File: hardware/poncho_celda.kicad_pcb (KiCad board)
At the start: 2 copper layers, 20 parts, among them U1 AD620, U2 REF1004-2.5, U3 ADS1113/15

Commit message: Primera version de de diseño de PCB, terminado.
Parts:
- moved C3 28.8 mm to (103.6, 115.2)
- moved R4 28.8 mm to (129.2, 138.6)
- moved U2 28.8 mm to (136.8, 132.2)
- moved C6 28.8 mm to (133.6, 122.0)
- moved C1 28.8 mm to (103.6, 118.5)
- moved C2 28.8 mm to (113.3, 124.6)
- moved C4 28.8 mm to (118.6, 123.1)
- moved R5 28.8 mm to (131.1, 108.3)
- moved U1 28.8 mm to (113.3, 117.0)
- moved U3 28.8 mm to (129.2, 117.0)
- moved R6 28.8 mm to (134.4, 108.3)
- moved C5 28.8 mm to (99.3, 139.1)
- moved R1 28.8 mm to (109.5, 130.9)
- moved R2 28.8 mm to (117.1, 130.9)
- moved R3 28.8 mm to (113.3, 111.1)
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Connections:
- R5 pad 1: +3.3V -> +3V3
- R6 pad 1: +3.3V -> +3V3
- XA1 pad 1: Net-(XA1-Pad1) -> +3V3
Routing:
- net +3V3: track 0.00 -> 38.9 mm
- net /lcd/RS: track 78.6 -> 106.6 mm, vias 2 -> 0
- net +5V: track 304.4 -> 281.4 mm
- net GND: track 251.9 -> 230.0 mm, vias 5 -> 3
- net /lcd/Ena: track 98.4 -> 120.1 mm
- net /ADC/sda: track 33.9 -> 44.8 mm, vias 0 -> 1
- net /ADC/alert: track 59.7 -> 50.2 mm, vias 0 -> 1
- net Net-(DS1-Pad16): track 6.73 -> 15.8 mm
- net /ADC/scl: track 28.1 -> 35.1 mm
- net /lcd/D2: track 65.9 -> 60.4 mm
- net /lcd/D1: track 68.6 -> 63.1 mm
- net /lcd/D4: track 59.0 -> 53.5 mm
- net /lcd/D3: track 63.0 -> 57.5 mm
- net Net-(DS1-Pad3): track 12.3 -> 10.8 mm
- added copper zone on F.Cu, net +5V
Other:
- board outline added: 85.9 x 137 mm

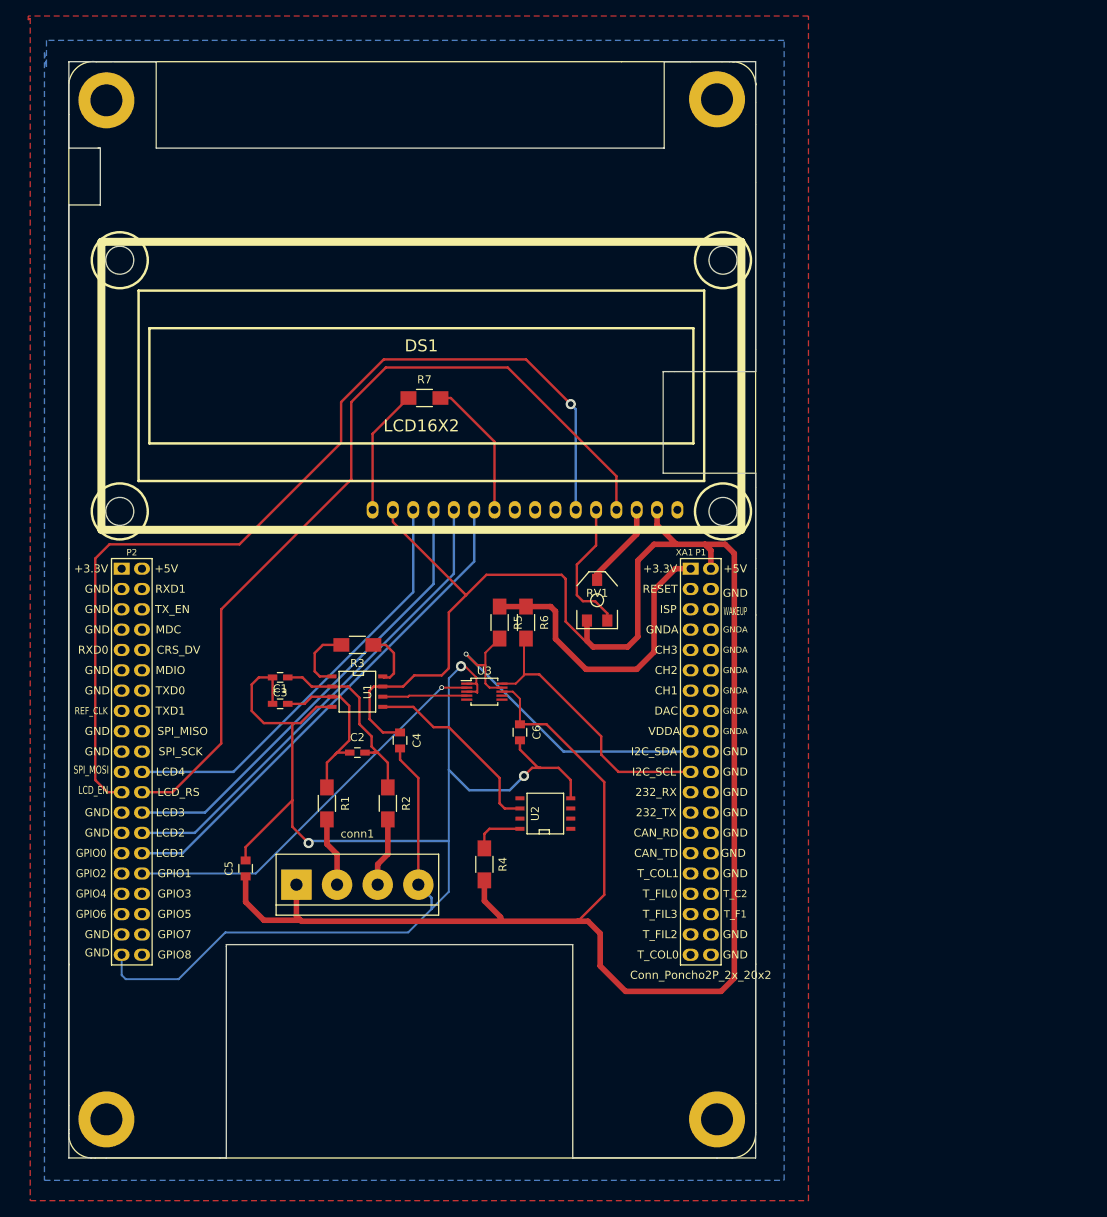
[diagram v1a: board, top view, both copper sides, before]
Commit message: Se realizan correcciones de PCB.
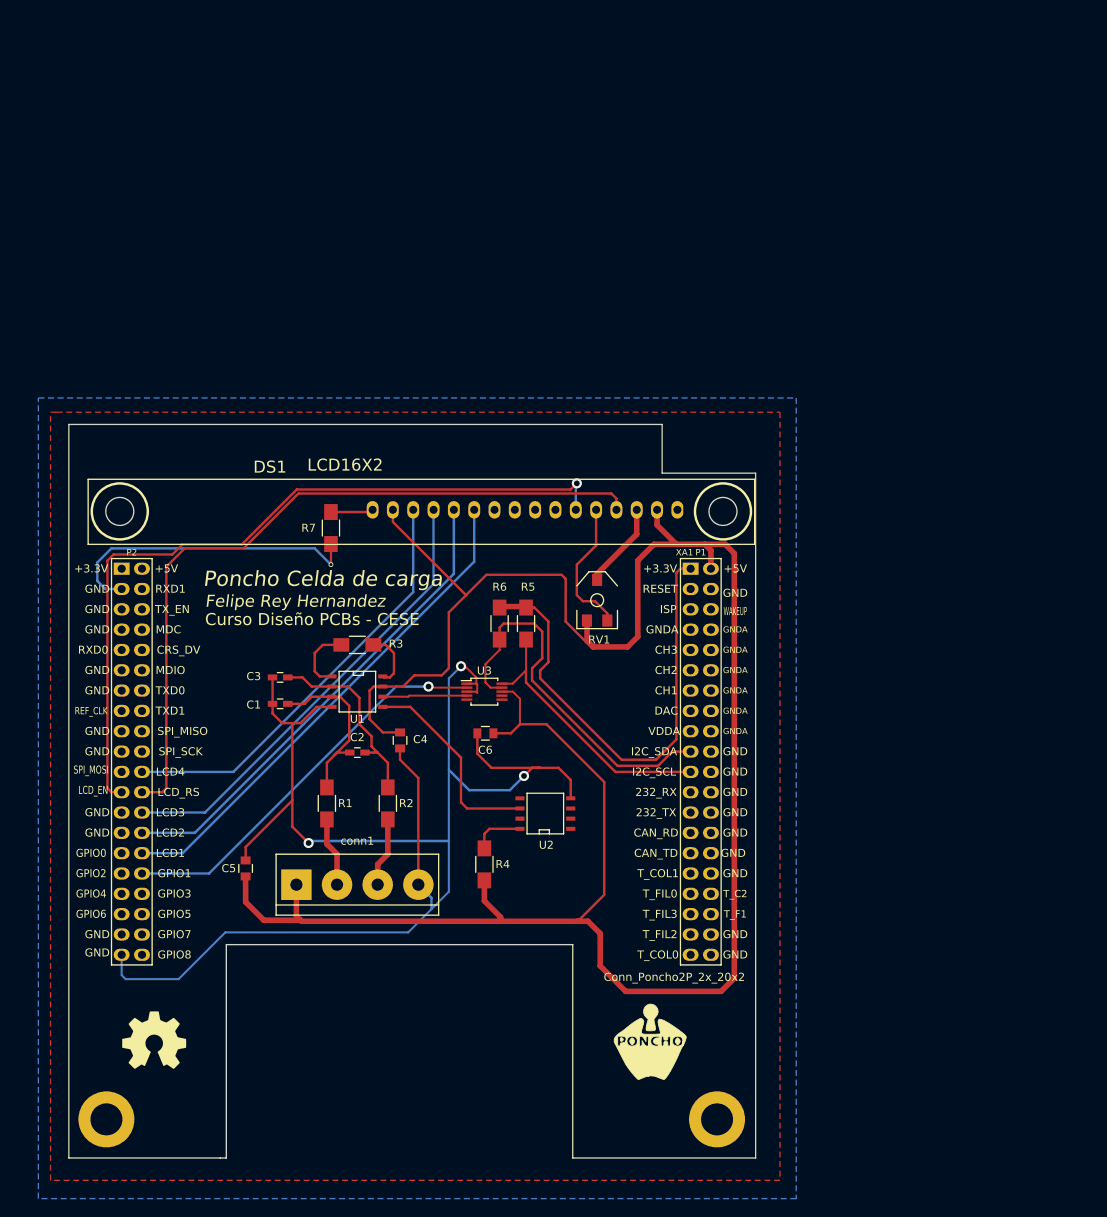
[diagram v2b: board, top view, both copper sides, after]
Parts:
- added G***: LOGO, celda:Logo_Poncho, F.Cu at (149.9, 160.8)
- added G101: Logo_OSHWA, celda:Logo_OSHWA, F.Cu at (87.9, 160.5)
- C1, C3: value 0.001uF -> 1nF
- C2: value 0.01uF -> 10nF
- C4, C5, C6: value 0.1uF -> 100nF
- DS1: footprint ej2cese:LCD16x2 -> celda:LCD16x2
- R1, R2: value 1326 -> 1k
- R3: value 500 -> 499
- R4: value 50k -> 51k
- RV1: value 10k -> 10K
- XA1: footprint ej2cese:PonchoGrande -> celda:PonchoGrande_sinBorde_ConHuecos
- moved R7 20.0 mm to (110.0, 96.5), turned to 270 degrees
- moved C6 4.32 mm to (129.3, 122.2), turned to 180 degrees
- moved R5 3.30 mm to (134.4, 108.5)
- moved R6 3.30 mm to (131.1, 108.5)
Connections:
- net /ADC/alert renamed /Adqui_Celda/alert
- net /ADC/celda_acond renamed Net-(U1-Pad6)
- net /lcd/D1 renamed /Conector-EDU_CIAA/lcd1
- net /lcd/D2 renamed /Conector-EDU_CIAA/lcd2
- net /lcd/D3 renamed /Conector-EDU_CIAA/lcd3
- net /lcd/D4 renamed /Conector-EDU_CIAA/lcd4
- net /lcd/Ena renamed /Conector-EDU_CIAA/lcdEn
- net /lcd/RS renamed /Conector-EDU_CIAA/lcdRs
- net celda+ renamed Net-(R1-Pad2)
- net celda- renamed Net-(R2-Pad2)
- net ref_2_5 renamed Net-(U1-Pad5)
- R5 pad 2: /ADC/sda -> /Adqui_Celda/scl
- R6 pad 2: /ADC/scl -> /Adqui_Celda/sda
- U3 pad 10: /ADC/scl -> /Adqui_Celda/scl
- U3 pad 9: /ADC/sda -> /Adqui_Celda/sda
- XA1 pad 19: /ADC/sda -> /Adqui_Celda/sda
- XA1 pad 21: /ADC/scl -> /Adqui_Celda/scl
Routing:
- net /Adqui_Celda/sda: track 0.00 -> 47.5 mm
- net /ADC/sda: track 44.8 -> 0.00 mm, vias 1 -> 0
- net /ADC/scl: track 35.1 -> 0.00 mm
- net /Adqui_Celda/scl: track 0.00 -> 34.6 mm
- net /Conector-EDU_CIAA/lcdEn: track 120.1 -> 96.5 mm
- net +3V3: track 38.9 -> 59.4 mm
- net GND: track 230.0 -> 250.3 mm, vias 3 -> 4
- net /Conector-EDU_CIAA/lcdRs: track 106.6 -> 92.7 mm
- net Net-(DS1-Pad16): track 15.8 -> 5.32 mm
- net +5V: track 281.4 -> 285.2 mm
- net Net-(U1-Pad5): track 24.3 -> 25.7 mm
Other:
- board size 85.9 x 137 mm -> 85.9 x 91.7 mm
- board text added: "Curso Diseño PCBs - CESE"
- board text added: "Felipe Rey Hernandez"
- board text added: "Poncho Celda de carga"

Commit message: Se agregan componentes 3d.
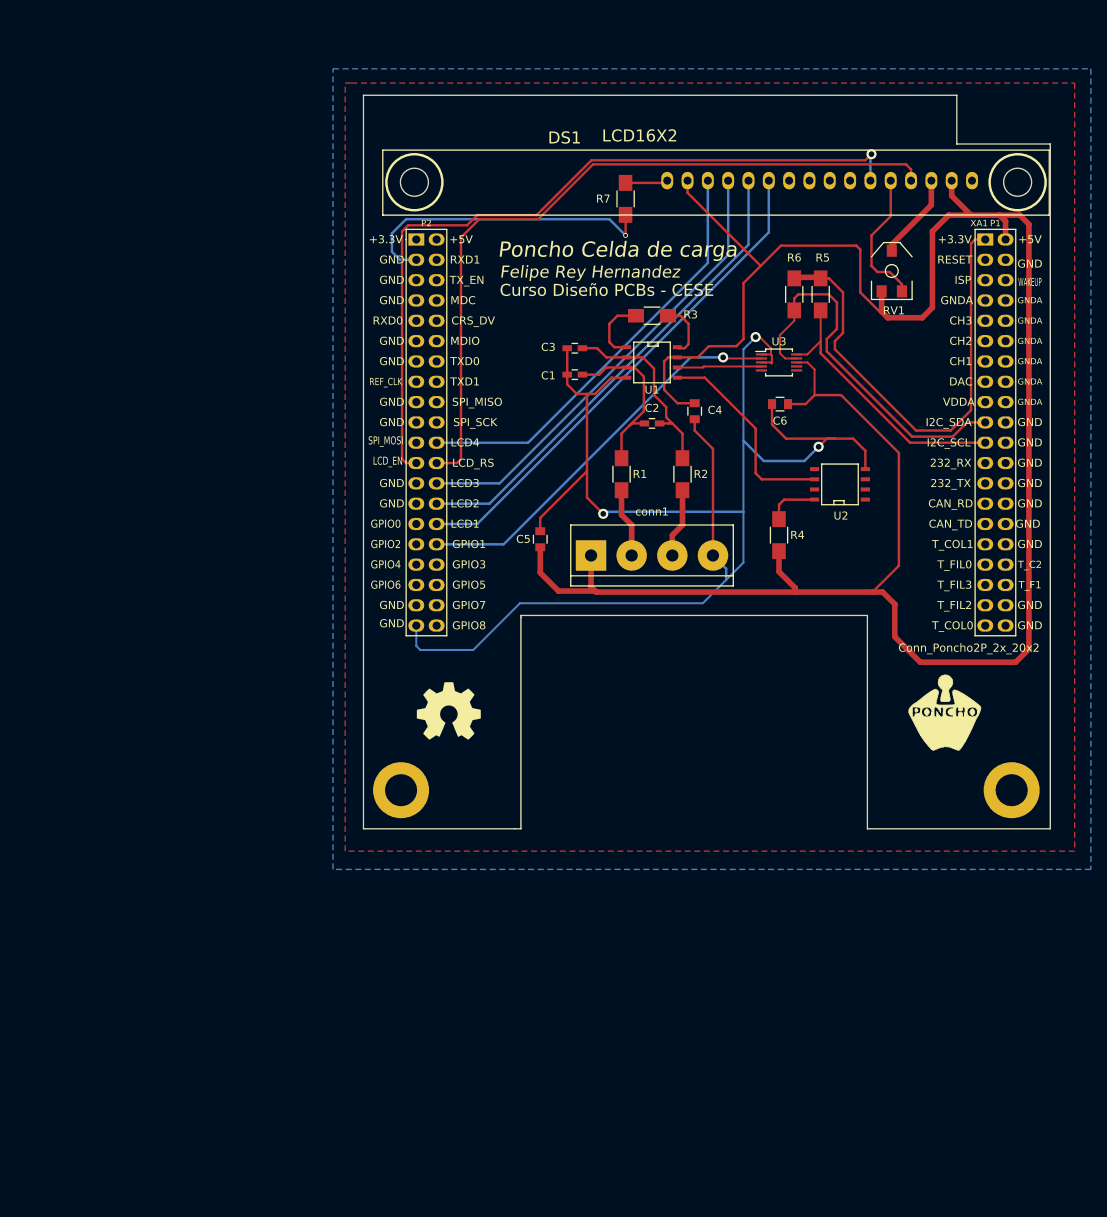
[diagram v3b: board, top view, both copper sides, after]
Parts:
- moved C6 55.2 mm to (166.1, 81.0)
- moved R2 55.2 mm to (153.9, 89.8)
- moved RV1 55.2 mm to (180.1, 64.4)
- moved C4 55.2 mm to (155.4, 81.9)
- moved C5 55.2 mm to (136.1, 97.9)
- moved DS1 55.2 mm to (158.1, 37.6)
- moved R6 55.2 mm to (167.9, 67.3)
- moved R7 55.2 mm to (146.8, 55.4)
- moved U2 55.2 mm to (173.6, 91.1)
- moved U3 55.2 mm to (166.0, 75.8)
- moved XA1 55.2 mm to (191.8, 60.5)
- moved C2 55.2 mm to (150.1, 83.4)
- moved G*** 55.2 mm to (186.7, 119.6)
- moved G101 55.2 mm to (124.7, 119.4)
- moved R1 55.2 mm to (146.3, 89.8)
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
